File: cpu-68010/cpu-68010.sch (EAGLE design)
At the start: 84 parts, among them IC10 74HC30D, IC11 74HC30D, IC12 74HC14D, IC13 MAX232, IC6 74HC00D, IC7 74HCT154DW, IC8 74HC04D, IC9 74HC148D, Q1 3.6864MHz, X1 FABC96R

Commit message: routed remaining signals between SRAM, added decoupling chips and more status LEDs
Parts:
- added LED10, LED7: YEL, led:LEDCHIPLED_1206
- added R14, R15, R16, R17, R18, R19, R20: 680R, rcl:R-EU_M0805
- added R5: 10k, rcl:R-EU_M0805
- C10, C15, C18, C22, C6: value 47µF -> 100nF; device rcl:CPOL-EUCT6032 -> rcl:C-EUC0805; MOUSER 581-TAJD476M016RNJV -> 710-885012207072
- C11, C19, C24, C40: value 100nF -> 47µF; device rcl:C-EUC0805 -> rcl:CPOL-EUCT6032; MOUSER 710-885012207072 -> 581-TAJD476M016RNJV
- C27: value 10µF -> 47µF; device rcl:CPOL-EUE1.8-4 -> rcl:CPOL-EUCT6032; MOUSER (none) -> 581-TAJD476M016RNJV
- C28, C29: value 10µF -> 100nF; device rcl:CPOL-EUE1.8-4 -> rcl:C-EUC0805; MOUSER (none) -> 710-885012207072
- C30: value 10µF -> 30pF; device rcl:CPOL-EUE1.8-4 -> rcl:C-EUC0805; MOUSER (none) -> 710-885012207072
- C32: value 30pF -> 47µF; device rcl:C-EUC0805 -> rcl:CPOL-EUCT6032; MOUSER 710-885012207072 -> 581-TAJD476M016RNJV
- C33, C35, C36: value 100nF -> 10µF; device rcl:C-EUC0805 -> rcl:CPOL-EUE1.8-4; MOUSER 710-885012207072 -> (none)
- C34: value 47µF -> 10µF; device rcl:CPOL-EUCT6032 -> rcl:CPOL-EUE1.8-4; MOUSER 581-TAJD476M016RNJV -> (none)
- IC10, IC11: value 74HC30D -> (none); device 74xx-eu:74HC30D -> 68komputer:CY62128BSOIC32
- IC12: value 74HC14D -> (none); device 74xx-eu:74HC14D -> 68komputer:SST39SF0X0PDIP32
- IC13: value MAX232 -> (none); device maxim:MAX232 -> 68komputer:SST39SF0X0PDIP32
- IC14: device 68komputer:CY62128BSOIC32 -> 68komputer:MC68681PLCC44-SOCKET
- IC15: device 68komputer:CY62128BSOIC32 -> 68komputer:DS1244EDIP-28
- IC16: value (none) -> MAX232; device 68komputer:CY62128BSOIC32 -> maxim:MAX232
- IC17: value (none) -> 74HC00D; device 68komputer:CY62128BSOIC32 -> 74xx-eu:74HC00D
- IC2: value (none) -> 74HC04D; device 68komputer:MC68681PLCC44-SOCKET -> 74xx-eu:74HC04D
- IC3: value (none) -> 74HCT154DW; device 68komputer:SST39SF0X0PDIP32 -> 74xx-eu:74HCT154DW
- IC4: value (none) -> 74HC30D; device 68komputer:SST39SF0X0PDIP32 -> 74xx-eu:74HC30D
- IC5: value (none) -> 74HC148D; device 68komputer:DS1244EDIP-28 -> 74xx-eu:74HC148D
- IC6: value 74HC00D -> 74HC30D; device 74xx-eu:74HC00D -> 74xx-eu:74HC30D
- IC7: value 74HCT154DW -> 74HC14D; device 74xx-eu:74HCT154DW -> 74xx-eu:74HC14D
- IC8: value 74HC04D -> (none); device 74xx-eu:74HC04D -> 68komputer:CY62128BSOIC32
- IC9: value 74HC148D -> (none); device 74xx-eu:74HC148D -> 68komputer:CY62128BSOIC32
- LED2, LED3: value GRN -> RED; MOUSER 604-APTR3216SGC -> 710-156120RS75300
- LED4, LED5, LED6, LED8, LED9: value GRN -> YEL; MOUSER 604-APTR3216SGC -> 710-156120YS75300
- R10, R11, R13, R4, R6: value 680R -> 10k
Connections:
- new net N$12: LED3.A, R2.2
- new net N$15: LED2.A, R1.2
- net !68681_CS: now also IC14.!CS, IC17A.O; no longer IC2.!CS, IC6A.O
- net !68681_DTACK: now also IC14.!DTACK, IC6A.I1, R9.2; no longer IC10A.I1, IC2.!DTACK
- net !68681_IRQ: now also IC14.!INTR, IC5A.5, R5.2; no longer IC2.!INTR, IC9A.5
- net !68681_IRQACK: now also IC14.!IACK; no longer IC2.!IACK
- net !A18: now also IC10.CE2, IC11.CE2, IC2E.O, IC8.CE2, IC9.CE2; no longer IC14.CE2, IC15.CE2, IC16.CE2, IC17.CE2, IC8E.O
- net !A19: now also IC17A.I1, IC2C.O; no longer IC6A.I1, IC8C.O
- net !DTACK: now also IC2D.O; no longer IC8D.O
- net !EXT_DTACK: now also IC6A.I0, R8.2; no longer IC10A.I0
- net !EXT_IRQ: now also IC5A.4, R4.2; no longer IC9A.4
- net !HALT: now also IC7B.O, LED2.C
- net !IPL0: now also IC5A.A0; no longer IC9A.A0
- net !IPL1: now also IC5A.A1; no longer IC9A.A1
- net !IPL2: now also IC5A.A2; no longer IC9A.A2
- net !NMI: now also IC5A.7, IC7A.O, R7.2; no longer IC12A.O, IC9A.7
- net !OE: now also IC10.!OE, IC11.!OE, IC12.!OE, IC13.!OE, IC2A.O, IC8.!OE, IC9.!OE; no longer IC14.!OE, IC16.!OE, IC17.!OE, IC3.!OE, IC4.!OE, IC5.!OE, IC8A.O
- net !REGION0: now also IC12.!CS, IC13.!CS, IC3A.0, IC6A.I2; no longer IC10A.I2, IC3.!CS, IC4.!CS, IC7A.0
- net !REGION1: now also IC10.!CE1, IC11.!CE1, IC3A.1, IC6A.I3, IC8.!CE1, IC9.!CE1; no longer IC10A.I3, IC14.!CE1, IC15.!CE1, IC16.!CE1, IC17.!CE1, IC7A.1
- net !REGION10: now also IC3A.10; no longer IC7A.10
- net !REGION11: now also IC3A.11; no longer IC7A.11
- net !REGION12: now also IC3A.12; no longer IC7A.12
- net !REGION13: now also IC3A.13; no longer IC7A.13
- net !REGION14: now also IC3A.14; no longer IC7A.14
- net !REGION15: now also IC2B.I, IC3A.15; no longer IC7A.15, IC8B.I
- net !REGION2: now also IC3A.2; no longer IC7A.2
- net !REGION3: now also IC3A.3; no longer IC7A.3
- net !REGION4: now also IC3A.4; no longer IC7A.4
- net !REGION5: now also IC3A.5; no longer IC7A.5
- net !REGION6: now also IC3A.6; no longer IC7A.6
- net !REGION7: now also IC3A.7; no longer IC7A.7
- net !REGION8: now also IC3A.8; no longer IC7A.8
- net !REGION9: now also IC3A.9; no longer IC7A.9
- net !RESET: now also IC14.!RESET, IC7C.O, LED3.C; no longer IC12C.O, IC2.!RESET
- net !RTC_CS: now also IC15.!CS, IC17B.O, IC6A.I4; no longer IC10A.I4, IC5.!CS, IC6B.O
- net !TIMER_IRQ: now also IC5A.6, R6.2; no longer IC9A.6
- net !VPA: now also IC4A.O; no longer IC11A.O
- net +5V: now also C10.1, C11.+, C15.1, C18.1, C19.+, C22.1, C24.+, C27.+, C28.1, C29.1, C32.+, C35.-, C37.1, C38.1, C40.+, C6.1, IC10.VCC, IC11.VCC, IC12.VCC, IC13.VCC, IC16P.VCC, IC17P.VCC, IC2P.VCC, IC3P.VCC, IC4A.I7, IC4P.VCC, IC5A.1, IC5A.2, IC5A.3, IC5P.VCC, IC6A.I5, IC6A.I6, IC6A.I7, IC8.VCC, IC9.VCC, R1.1, R2.1, R3.1, R4.1, R8.1, R9.1; no longer C10.+, C11.1, C12.1, C13.1, C15.+, C18.+, C19.1, C22.+, C24.1, C27.-, C33.1, C34.+, C35.1, C36.1, C40.1, C6.+, IC10A.I5, IC10A.I6, IC10A.I7, IC10P.VCC, IC11A.I7, IC11P.VCC, IC12P.VCC, IC13P.VCC, IC16.VCC, IC17.VCC, IC2.VCC, IC3.VCC, IC4.VCC, IC5.VCC, IC8P.VCC, IC9A.1, IC9A.2, IC9A.3, IC9P.VCC, R13.1
- net /AS: now also IC3A.G1, IC3A.G2; no longer IC7A.G1, IC7A.G2
- net 68681_XTAL1: now also C30.1, IC14.X1/CLK; no longer C31.1, IC2.X1/CLK
- net 68681_XTAL2: now also C31.2, IC14.X2; no longer C32.2, IC2.X2
- net A1: now also IC10.A0, IC11.A0, IC12.A0, IC13.A0, IC14.A1, IC8.A0, IC9.A0; no longer IC14.A0, IC16.A0, IC17.A0, IC2.A1, IC3.A0, IC4.A0, IC5.A0
- net A10: now also IC10.A9, IC11.A9, IC12.A9, IC13.A9, IC8.A9, IC9.A9; no longer IC14.A9, IC16.A9, IC17.A9, IC3.A9, IC4.A9, IC5.A9
- net A11: now also IC10.A10, IC11.A10, IC12.A10, IC13.A10, IC8.A10, IC9.A10; no longer IC14.A10, IC16.A10, IC17.A10, IC3.A10, IC4.A10, IC5.A10
- net A12: now also IC10.A11, IC11.A11, IC12.A11, IC13.A11, IC8.A11, IC9.A11; no longer IC14.A11, IC16.A11, IC17.A11, IC3.A11, IC4.A11, IC5.A11
- net A13: now also IC10.A12, IC11.A12, IC12.A12, IC13.A12, IC8.A12, IC9.A12; no longer IC14.A12, IC16.A12, IC17.A12, IC3.A12, IC4.A12, IC5.A12
- net A14: now also IC10.A13, IC11.A13, IC12.A13, IC13.A13, IC8.A13, IC9.A13; no longer IC14.A13, IC16.A13, IC17.A13, IC3.A13, IC4.A13, IC5.A13
- net A15: now also IC10.A14, IC11.A14, IC12.A14, IC13.A14, IC8.A14, IC9.A14; no longer IC14.A14, IC16.A14, IC17.A14, IC3.A14, IC4.A14, IC5.A14
- net A16: now also IC10.A15, IC11.A15, IC12.A15, IC13.A15, IC4A.I3, IC8.A15, IC9.A15; no longer IC11A.I3, IC14.A15, IC15.A15, IC16.A15, IC17.A15, IC3.A15, IC4.A15
- net A17: now also IC10.A16, IC11.A16, IC12.A16, IC13.A16, IC4A.I4, IC8.A16, IC9.A16; no longer IC11A.I4, IC14.A16, IC15.A16, IC16.A16, IC17.A16, IC3.A16, IC4.A16
- net A18: now also IC12.A17, IC13.A17, IC2E.I, IC4A.I5; no longer IC11A.I5, IC3.A17, IC4.A17, IC8E.I
- net A19: now also IC12.A18, IC13.A18, IC17B.I1, IC2C.I, IC4A.I6; no longer IC11A.I6, IC3.A18, IC4.A18, IC6B.I1, IC8C.I
- net A2: now also IC10.A1, IC11.A1, IC12.A1, IC13.A1, IC14.A2, IC8.A1, IC9.A1; no longer IC14.A1, IC16.A1, IC17.A1, IC2.A2, IC3.A1, IC4.A1, IC5.A1
- net A20: now also IC3A.A; no longer IC7A.A
- net A21: now also IC3A.B; no longer IC7A.B
- net A22: now also IC3A.C; no longer IC7A.C
- net A23: now also IC3A.D; no longer IC7A.D
- net A3: now also IC10.A2, IC11.A2, IC12.A2, IC13.A2, IC14.A3, IC8.A2, IC9.A2; no longer IC14.A2, IC16.A2, IC17.A2, IC2.A3, IC3.A2, IC4.A2, IC5.A2
- net A4: now also IC10.A3, IC11.A3, IC12.A3, IC13.A3, IC14.A4, IC8.A3, IC9.A3; no longer IC14.A3, IC16.A3, IC17.A3, IC2.A4, IC3.A3, IC4.A3, IC5.A3
- net A5: now also IC10.A4, IC11.A4, IC12.A4, IC13.A4, IC8.A4, IC9.A4; no longer IC14.A4, IC16.A4, IC17.A4, IC3.A4, IC4.A4, IC5.A4
- net A6: now also IC10.A5, IC11.A5, IC12.A5, IC13.A5, IC8.A5, IC9.A5; no longer IC14.A5, IC16.A5, IC17.A5, IC3.A5, IC4.A5, IC5.A5
- net A7: now also IC10.A6, IC11.A6, IC12.A6, IC13.A6, IC8.A6, IC9.A6; no longer IC14.A6, IC16.A6, IC17.A6, IC3.A6, IC4.A6, IC5.A6
- net A8: now also IC10.A7, IC11.A7, IC12.A7, IC13.A7, IC8.A7, IC9.A7; no longer IC14.A7, IC16.A7, IC17.A7, IC3.A7, IC4.A7, IC5.A7
- net A9: now also IC10.A8, IC11.A8, IC12.A8, IC13.A8, IC8.A8, IC9.A8; no longer IC14.A8, IC16.A8, IC17.A8, IC3.A8, IC4.A8, IC5.A8
- net D0: now also IC10.D0, IC11.D0, IC13.DQ0, IC14.D0, IC15.DQ0; no longer IC15.D0, IC17.D0, IC2.D0, IC4.DQ0, IC5.DQ0
- net D1: now also IC10.D1, IC11.D1, IC13.DQ1, IC14.D1, IC15.DQ1; no longer IC15.D1, IC17.D1, IC2.D1, IC4.DQ1, IC5.DQ1
- net D10: now also IC12.DQ2, IC8.D2, IC9.D2; no longer IC14.D2, IC16.D2, IC3.DQ2
- net D11: now also IC12.DQ3, IC8.D3, IC9.D3; no longer IC14.D3, IC16.D3, IC3.DQ3
- net D12: now also IC12.DQ4, IC8.D4, IC9.D4; no longer IC14.D4, IC16.D4, IC3.DQ4
- net D13: now also IC12.DQ5, IC8.D5, IC9.D5; no longer IC14.D5, IC16.D5, IC3.DQ5
- net D14: now also IC12.DQ6, IC8.D6, IC9.D6; no longer IC14.D6, IC16.D6, IC3.DQ6
- net D15: now also IC12.DQ7, IC8.D7, IC9.D7; no longer IC14.D7, IC16.D7, IC3.DQ7
- net D2: now also IC10.D2, IC11.D2, IC13.DQ2, IC14.D2, IC15.DQ2; no longer IC15.D2, IC17.D2, IC2.D2, IC4.DQ2, IC5.DQ2
- net D3: now also IC10.D3, IC11.D3, IC13.DQ3, IC14.D3, IC15.DQ3; no longer IC15.D3, IC17.D3, IC2.D3, IC4.DQ3, IC5.DQ3
- net D4: now also IC10.D4, IC11.D4, IC13.DQ4, IC14.D4, IC15.DQ4; no longer IC15.D4, IC17.D4, IC2.D4, IC4.DQ4, IC5.DQ4
- net D5: now also IC10.D5, IC11.D5, IC13.DQ5, IC14.D5, IC15.DQ5; no longer IC15.D5, IC17.D5, IC2.D5, IC4.DQ5, IC5.DQ5
- net D6: now also IC10.D6, IC11.D6, IC13.DQ6, IC14.D6, IC15.DQ6; no longer IC15.D6, IC17.D6, IC2.D6, IC4.DQ6, IC5.DQ6
- net D7: now also IC10.D7, IC11.D7, IC13.DQ7, IC14.D7, IC15.DQ7; no longer IC15.D7, IC17.D7, IC2.D7, IC4.DQ7, IC5.DQ7
- net D8: now also IC12.DQ0, IC8.D0, IC9.D0; no longer IC14.D0, IC16.D0, IC3.DQ0
- net D9: now also IC12.DQ1, IC8.D1, IC9.D1; no longer IC14.D1, IC16.D1, IC3.DQ1
- net DTACK: now also IC2D.I, IC6A.O; no longer IC10A.O, IC8D.I
- net FC0: now also IC4A.I0; no longer IC11A.I0
- net FC1: now also IC4A.I1; no longer IC11A.I1
- net FC2: now also IC4A.I2; no longer IC11A.I2
- net GND: now also C10.2, C11.-, C15.2, C18.2, C19.-, C22.2, C24.-, C27.-, C28.2, C29.2, C30.2, C31.1, C32.-, C36.+, C40.-, C6.2, IC10.GND, IC11.GND, IC12.GND, IC13.GND, IC16P.GND, IC17P.GND, IC2P.GND, IC3P.GND, IC4P.GND, IC5A.0, IC5A.EI, IC5P.GND, IC8.GND, IC9.GND, LED1.C, LED10.C, LED4.C, LED5.C, LED7.C, R13.2; no longer C10.-, C11.2, C15.-, C18.-, C19.2, C22.-, C24.2, C28.+, C31.2, C32.1, C33.2, C34.-, C35.2, C36.2, C40.2, C6.-, IC10P.GND, IC11P.GND, IC12P.GND, IC13P.GND, IC16.GND, IC17.GND, IC2.GND, IC3.GND, IC4.GND, IC5.GND, IC8P.GND, IC9A.0, IC9A.EI, IC9P.GND, R9.2
- net GPIO_IN0: now also IC14.IP0; no longer IC2.IP0
- net GPIO_IN1: now also IC14.IP1; no longer IC2.IP1
- net GPIO_IN2: now also IC14.IP2; no longer IC2.IP2
- net GPIO_IN3: now also IC14.IP3; no longer IC2.IP3
- net GPIO_IN4: now also IC14.IP4; no longer IC2.IP4
- net GPIO_IN5: now also IC14.IP5; no longer IC2.IP5
- net GPIO_OUT0: now also IC14.OP0, R14.1; no longer IC2.OP0, R4.1
- net GPIO_OUT1: now also IC14.OP1, R15.1; no longer IC2.OP1, R3.1
- net GPIO_OUT2: now also IC14.OP3, R16.1; no longer IC2.OP3, R2.1
- net GPIO_OUT3: now also IC14.OP4, R17.1; no longer IC2.OP4, R1.1
- net GPIO_OUT4: now also IC14.OP5, R18.1; no longer IC2.OP5, R11.1
- net GPIO_OUT5: now also IC14.OP6, R19.1; no longer IC2.OP6, R10.1
- net GPIO_OUT6: now also IC14.OP7, R20.1; no longer IC2.OP7, R6.1
- net N$1: now also C35.+, IC16G$1.V+; no longer C27.+, IC13G$1.V+
- net N$10: now also LED7.A, R17.2; no longer LED1.A, R1.2
- net N$11: now also LED6.A, R16.2; no longer LED2.A, R2.2
- net N$13: now also R15.2; no longer R3.2
- net N$14: now also LED4.A, R14.2; no longer LED6.A, R4.2
- net N$17: now also LED10.A, R20.2; no longer LED8.A, R6.2
- net N$18: now also R10.2; no longer R7.2
- net N$19: now also LED1.A, R3.2; no longer LED9.A, R13.2
- net N$2: now also C36.-, IC16G$1.V-; no longer C28.-, IC13G$1.V-
- net N$3: now also C33.+, IC16G$1.C1+; no longer C29.+, IC13G$1.C1+
- net N$4: now also C34.+, IC16G$1.C2+; no longer C30.+, IC13G$1.C2+
- net N$5: now also C33.-, IC16G$1.C1-; no longer C29.-, IC13G$1.C1-
- net N$6: now also C34.-, IC16G$1.C2-; no longer C30.-, IC13G$1.C2-
- net N$7: now also LED9.A, R19.2; no longer LED3.A, R10.2
- net N$8: now also LED8.A, R18.2; no longer LED4.A, R11.2
- net N$9: now also R11.2; no longer R8.2
- net NMI_SW: now also C12.1, IC7A.I, R10.1; no longer C37.1, IC12A.I, R7.1
- net R!W!: now also IC2A.I; no longer IC8A.I
- net R/!W!: now also IC10.!WE, IC11.!WE, IC12.!WE, IC13.!WE, IC14.R/!W, IC8.!WE, IC9.!WE; no longer IC14.!WE, IC16.!WE, IC17.!WE, IC2.R/!W, IC3.!WE, IC4.!WE, IC5.!WE
- net REGION15: now also IC17A.I0, IC17B.I0, IC2B.O; no longer IC6A.I0, IC6B.I0, IC8B.O
- net RESET_SW: now also C13.1, IC7B.I, IC7C.I, R11.1, R13.1; no longer C38.1, IC12C.I, R8.1, R9.1
- net RS232_0_RX: now also IC16G$1.T1OUT; no longer IC13G$1.T1OUT
- net RS232_0_TX: now also IC16G$1.R1IN; no longer IC13G$1.R1IN
- net RS232_1_RX: now also IC16G$1.T2OUT; no longer IC13G$1.T2OUT
- net RS232_1_TX: now also IC16G$1.R2IN; no longer IC13G$1.R2IN
- net TIMER_CLK: now also IC14.OP2; no longer IC2.OP2
- net UART0_RX: now also IC14.RXDA, IC16G$1.R1OUT; no longer IC13G$1.R1OUT, IC2.RXDA
- net UART0_TX: now also IC14.TXDA, IC16G$1.T1IN; no longer IC13G$1.T1IN, IC2.TXDA
- net UART1_RX: now also IC14.RXDB, IC16G$1.R2OUT; no longer IC13G$1.R2OUT, IC2.RXDB
- net UART1_TX: now also IC14.TXDB, IC16G$1.T2IN; no longer IC13G$1.T2IN, IC2.TXDB

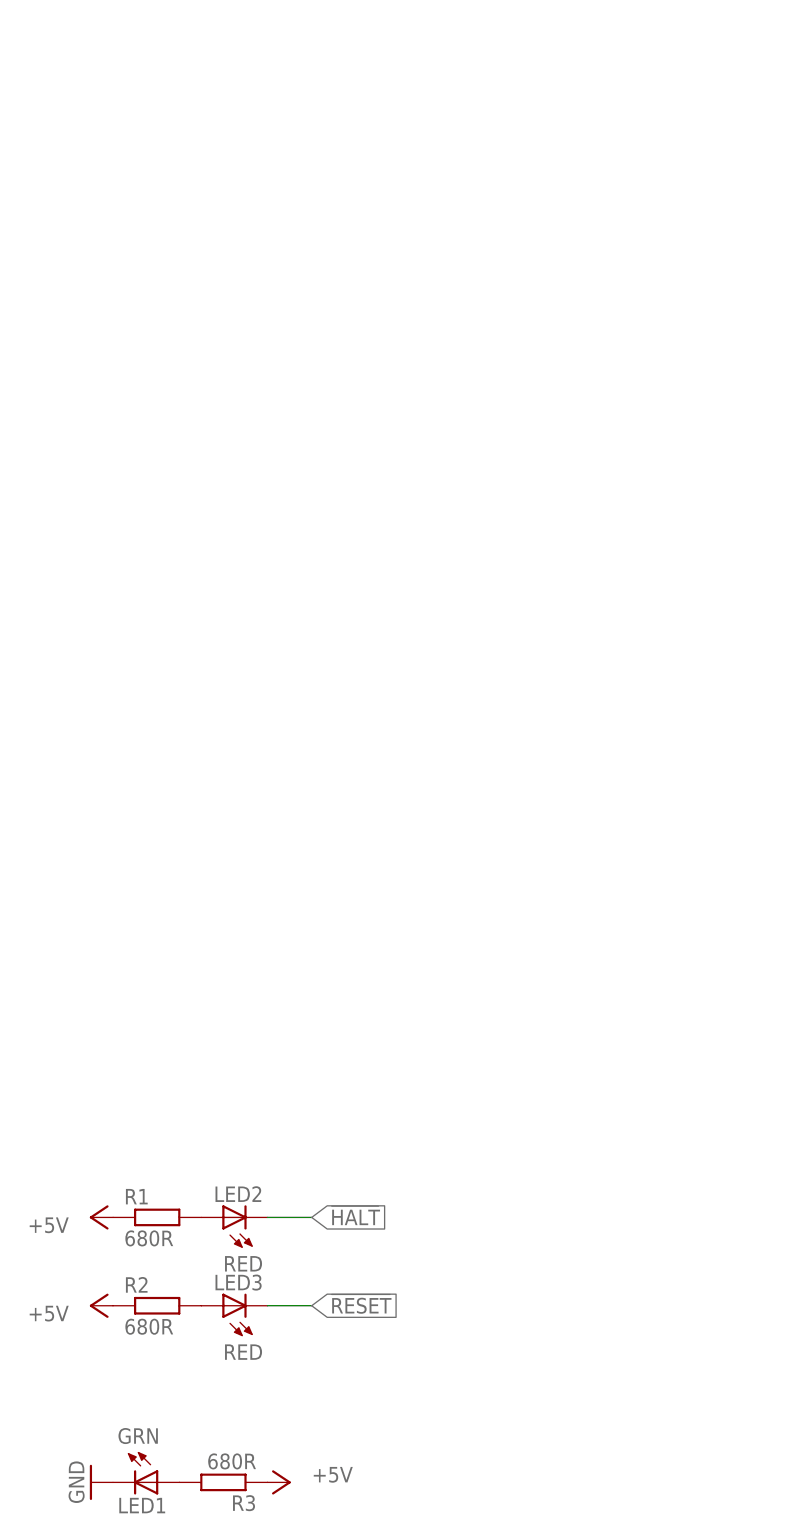
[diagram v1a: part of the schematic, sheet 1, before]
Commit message: routed more signals, added power connector
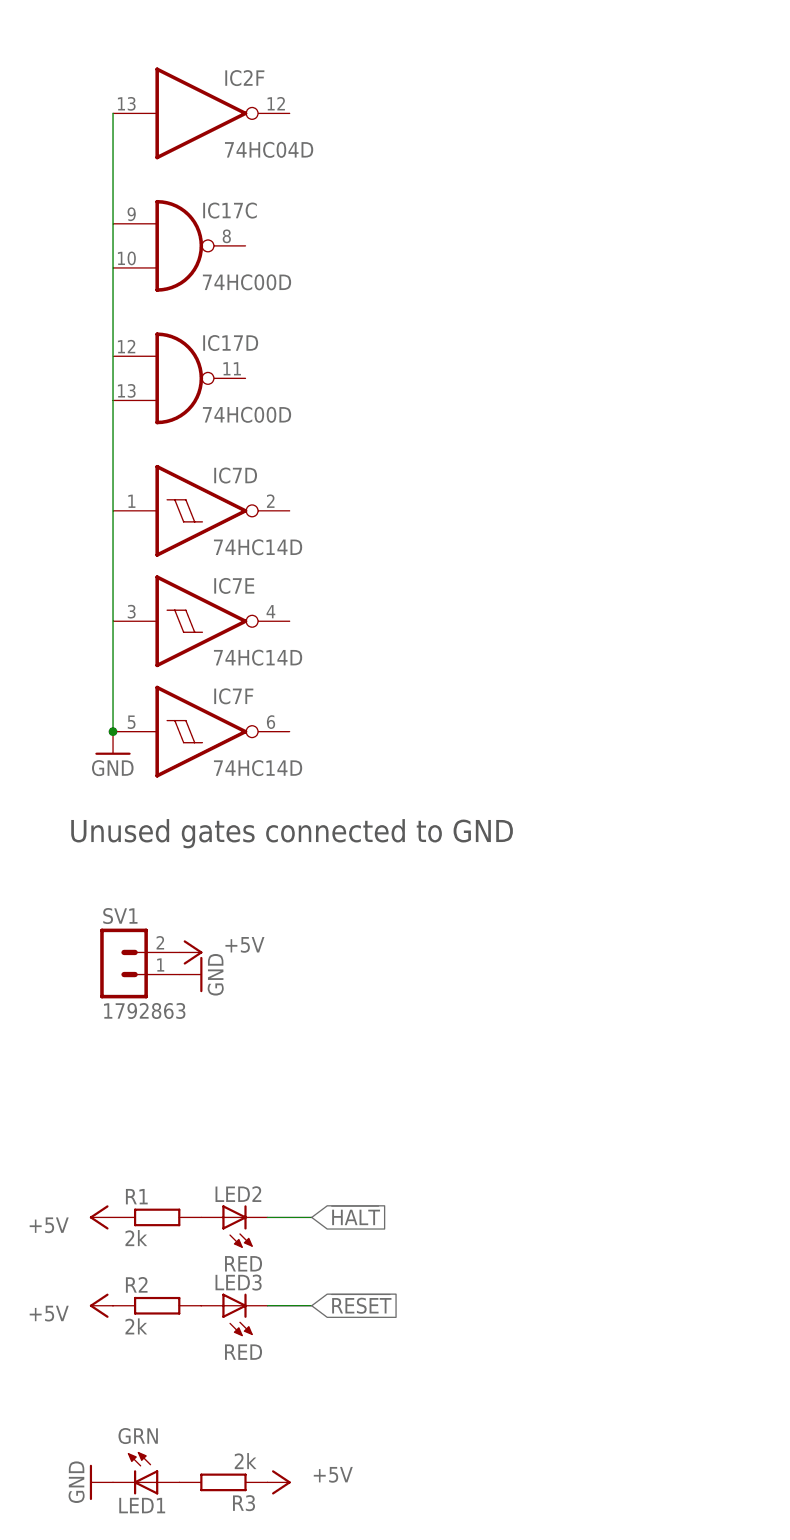
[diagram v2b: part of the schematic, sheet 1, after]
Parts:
- added SV1: 1792863, 68komputer:1792863
- R1, R14, R15, R16, R17, R18, R19, R2, R20, R3: value 680R -> 2k
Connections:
- net +5V: now also SV1.2
- net GND: now also IC2F.I, IC7F.I, SV1.1
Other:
- note added: "IC15 should be socketed (28 pin DIP)"
- note added: "ROM is decoded for $000000-$0FFFFF (1MB) No waitstates are inserted IC12, IC13 should be socketed (32 pin DIP)"
- note added: "Unused gates connected to GND"
- note removed: "ROM is decoded for $000000-$0FFFFF (1MB) No waitstates are inserted"
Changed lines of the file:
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@@
 <attribute name="MOUSER" value="710-156120YS75300"/>
 </part>
-<part name="R19" library="rcl" library_urn="urn:adsk.eagle:library:334" deviceset="R-EU_" device="M0805" package3d_urn="urn:adsk.eagle:package:23556/1" value="680R">
+<part name="R19" library="rcl" library_urn="urn:adsk.eagle:library:334" deviceset="R-EU_" device="M0805" package3d_urn="urn:adsk.eagle:package:23556/1" value="2k">
 <attribute name="MOUSER" value="652-CR0805-FX6800GLF"/>
 </part>
-<part name="R18" library="rcl" library_urn="urn:adsk.eagle:library:334" deviceset="R-EU_" device="M0805" package3d_urn="urn:adsk.eagle:package:23556/1" value="680R">
+<part name="R18" library="rcl" library_urn="urn:adsk.eagle:library:334" deviceset="R-EU_" device="M0805" package3d_urn="urn:adsk.eagle:package:23556/1" value="2k">
 <attribute name="MOUSER" value="652-CR0805-FX6800GLF"/>
 </part>
@@
 <attribute name="MOUSER" value="710-156120YS75300"/>
 </part>
-<part name="R17" library="rcl" library_urn="urn:adsk.eagle:library:334" deviceset="R-EU_" device="M0805" package3d_urn="urn:adsk.eagle:package:23556/1" value="680R">
+<part name="R17" library="rcl" library_urn="urn:adsk.eagle:library:334" deviceset="R-EU_" device="M0805" package3d_urn="urn:adsk.eagle:package:23556/1" value="2k">
 <attribute name="MOUSER" value="652-CR0805-FX6800GLF"/>
 </part>
-<part name="R16" library="rcl" library_urn="urn:adsk.eagle:library:334" deviceset="R-EU_" device="M0805" package3d_urn="urn:adsk.eagle:package:23556/1" value="680R">
+<part name="R16" library="rcl" library_urn="urn:adsk.eagle:library:334" deviceset="R-EU_" device="M0805" package3d_urn="urn:adsk.eagle:package:23556/1" value="2k">
 <attribute name="MOUSER" value="652-CR0805-FX6800GLF"/>
 </part>
@@
 <attribute name="MOUSER" value="710-156120YS75300"/>
 </part>
-<part name="R15" library="rcl" library_urn="urn:adsk.eagle:library:334" deviceset="R-EU_" device="M0805" package3d_urn="urn:adsk.eagle:package:23556/1" value="680R">
+<part name="R15" library="rcl" library_urn="urn:adsk.eagle:library:334" deviceset="R-EU_" device="M0805" package3d_urn="urn:adsk.eagle:package:23556/1" value="2k">
 <attribute name="MOUSER" value="652-CR0805-FX6800GLF"/>
 </part>
-<part name="R14" library="rcl" library_urn="urn:adsk.eagle:library:334" deviceset="R-EU_" device="M0805" package3d_urn="urn:adsk.eagle:package:23556/1" value="680R">
+<part name="R14" library="rcl" library_urn="urn:adsk.eagle:library:334" deviceset="R-EU_" device="M0805" package3d_urn="urn:adsk.eagle:package:23556/1" value="2k">
 <attribute name="MOUSER" value="652-CR0805-FX6800GLF"/>
 </part>
@@
 <attribute name="MOUSER" value="710-156120YS75300"/>
 </part>
-<part name="R20" library="rcl" library_urn="urn:adsk.eagle:library:334" deviceset="R-EU_" device="M0805" package3d_urn="urn:adsk.eagle:package:23556/1" value="680R">
+<part name="R20" library="rcl" library_urn="urn:adsk.eagle:library:334" deviceset="R-EU_" device="M0805" package3d_urn="urn:adsk.eagle:package:23556/1" value="2k">
 <attribute name="MOUSER" value="652-CR0805-FX6800GLF"/>
 </part>
@@
 <attribute name="MOUSER" value="710-885012207072"/>
 </part>
-<part name="R3" library="rcl" library_urn="urn:adsk.eagle:library:334" deviceset="R-EU_" device="M0805" package3d_urn="urn:adsk.eagle:package:23556/1" value="680R">
+<part name="R3" library="rcl" library_urn="urn:adsk.eagle:library:334" deviceset="R-EU_" device="M0805" package3d_urn="urn:adsk.eagle:package:23556/1" value="2k">
 <attribute name="MOUSER" value="652-CR0805-FX6800GLF"/>
 </part>
@@
 </part>
 <part name="P+14" library="supply1" library_urn="urn:adsk.eagle:library:371" deviceset="+5V" device=""/>
-<part name="R2" library="rcl" library_urn="urn:adsk.eagle:library:334" deviceset="R-EU_" device="M0805" package3d_urn="urn:adsk.eagle:package:23556/1" value="680R">
+<part name="R2" library="rcl" library_urn="urn:adsk.eagle:library:334" deviceset="R-EU_" device="M0805" package3d_urn="urn:adsk.eagle:package:23556/1" value="2k">
 <attribute name="MOUSER" value="652-CR0805-FX6800GLF"/>
 </part>
@@
 </part>
 <part name="P+2" library="supply1" library_urn="urn:adsk.eagle:library:371" deviceset="+5V" device=""/>
-<part name="R1" library="rcl" library_urn="urn:adsk.eagle:library:334" deviceset="R-EU_" device="M0805" package3d_urn="urn:adsk.eagle:package:23556/1" value="680R">
+<part name="R1" library="rcl" library_urn="urn:adsk.eagle:library:334" deviceset="R-EU_" device="M0805" package3d_urn="urn:adsk.eagle:package:23556/1" value="2k">
 <attribute name="MOUSER" value="652-CR0805-FX6800GLF"/>
 </part>
@@
 </part>
 <part name="P+1" library="supply1" library_urn="urn:adsk.eagle:library:371" deviceset="+5V" device=""/>
+<part name="SV1" library="68komputer" deviceset="1792863" device=""/>
+<part name="P+32" library="supply1" library_urn="urn:adsk.eagle:library:371" deviceset="+5V" device=""/>
+<part name="GND41" library="supply1" library_urn="urn:adsk.eagle:library:371" deviceset="GND" device=""/>
+<part name="GND42" library="supply1" library_urn="urn:adsk.eagle:library:371" deviceset="GND" device=""/>
 </parts>
 <sheets>
@@
 <plain>
 <text x="215.9" y="81.28" size="2.54" layer="97" align="top-center">External bus I/F</text>
+<text x="5.08" y="88.9" size="2.54" layer="97">Unused gates connected to GND</text>
 </plain>
 <instances>
@@
 <attribute name="VALUE" x="5.08" y="45.72" size="1.778" layer="96" rot="R180"/>
 </instance>
+<instance part="SV1" gate="G$1" x="10.16" y="76.2" smashed="yes">
+<attribute name="VALUE" x="8.89" y="68.58" size="1.778" layer="96"/>
+<attribute name="NAME" x="8.89" y="79.502" size="1.778" layer="95"/>
+</instance>
+<instance part="P+32" gate="1" x="20.32" y="76.2" smashed="yes" rot="R270">
+<attribute name="VALUE" x="22.86" y="76.2" size="1.778" layer="96"/>
+</instance>
+<instance part="GND41" gate="1" x="20.32" y="73.66" smashed="yes" rot="R90">
+<attribute name="VALUE" x="22.86" y="71.12" size="1.778" layer="96" rot="R90"/>
+</instance>
+<instance part="IC2" gate="F" x="20.32" y="172.72" smashed="yes">
+<attribute name="NAME" x="22.86" y="175.895" size="1.778" layer="95"/>
+<attribute name="VALUE" x="22.86" y="167.64" size="1.778" layer="96"/>
+</instance>
+<instance part="IC17" gate="C" x="17.78" y="157.48" smashed="yes">
+<attribute name="NAME" x="20.32" y="160.655" size="1.778" layer="95"/>
+<attribute name="VALUE" x="20.32" y="152.4" size="1.778" layer="96"/>
+</instance>
+<instance part="IC17" gate="D" x="17.78" y="142.24" smashed="yes">
+<attribute name="NAME" x="20.32" y="145.415" size="1.778" layer="95"/>
+<attribute name="VALUE" x="20.32" y="137.16" size="1.778" layer="96"/>
+</instance>
+<instance part="IC7" gate="D" x="20.32" y="127" smashed="yes">
+<attribute name="NAME" x="21.59" y="130.175" size="1.778" layer="95"/>
+<attribute name="VALUE" x="21.59" y="121.92" size="1.778" layer="96"/>
+</instance>
+<instance part="IC7" gate="E" x="20.32" y="114.3" smashed="yes">
+<attribute name="NAME" x="21.59" y="117.475" size="1.778" layer="95"/>
+<attribute name="VALUE" x="21.59" y="109.22" size="1.778" layer="96"/>
+</instance>
+<instance part="IC7" gate="F" x="20.32" y="101.6" smashed="yes">
+<attribute name="NAME" x="21.59" y="104.775" size="1.778" layer="95"/>
+<attribute name="VALUE" x="21.59" y="96.52" size="1.778" layer="96"/>
+</instance>
+<instance part="GND42" gate="1" x="10.16" y="99.06" smashed="yes">
+<attribute name="VALUE" x="7.62" y="96.52" size="1.778" layer="96"/>
+</instance>
 </instances>
 <busses>
@@
 <pinref part="P+1" gate="1" pin="+5V"/>
 </segment>
+<segment>
+<pinref part="SV1" gate="G$1" pin="2"/>
+<pinref part="P+32" gate="1" pin="+5V"/>
+</segment>
 </net>
 <net name="GND" class="0">
@@
 <pinref part="GND1" gate="1" pin="GND"/>
 </segment>
+<segment>
+<pinref part="SV1" gate="G$1" pin="1"/>
+<pinref part="GND41" gate="1" pin="GND"/>
+</segment>
+<segment>
+<pinref part="IC2" gate="F" pin="I"/>
+<pinref part="IC7" gate="F" pin="I"/>
+<wire x1="10.16" y1="172.72" x2="10.16" y2="101.6" width="0.1524" layer="91"/>
+<pinref part="GND42" gate="1" pin="GND"/>
+<junction x="10.16" y="101.6"/>
+</segment>
 </net>
 <net name="A1" class="0">
@@
 <text x="33.02" y="177.8" size="1.778" layer="97" align="bottom-center">High ROM</text>
 <text x="86.36" y="177.8" size="1.778" layer="97" align="bottom-center">Low ROM</text>
-<text x="149.86" y="33.02" size="2.54" layer="94" align="top-left">ROM is decoded for $000000-$0FFFFF (1MB)
-No waitstates are inserted</text>
+<text x="149.86" y="34.29" size="2.54" layer="94" align="top-left">ROM is decoded for $000000-$0FFFFF (1MB)
+No waitstates are inserted
+IC12, IC13 should be socketed (32 pin DIP)</text>
 <text x="60.96" y="104.14" size="1.778" layer="97" align="top-center">IC3/IC4 can be one of SST39SF0[1,2,4]0</text>
 </plain>
@@
 /RTC_CS: ~(A[19] &amp; ~REGION[15])</text>
 <wire x1="73.66" y1="35.56" x2="0" y2="35.56" width="0.1524" layer="94"/>
+<text x="149.86" y="33.02" size="2.54" layer="94" align="top-left">IC15 should be socketed (28 pin DIP)</text>
 </plain>
 <instances>
